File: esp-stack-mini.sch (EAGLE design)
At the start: 43 parts, among them IC1 FT232RL, Q1 200mA/50V, U1 TPS737XX, U2 MCP73831

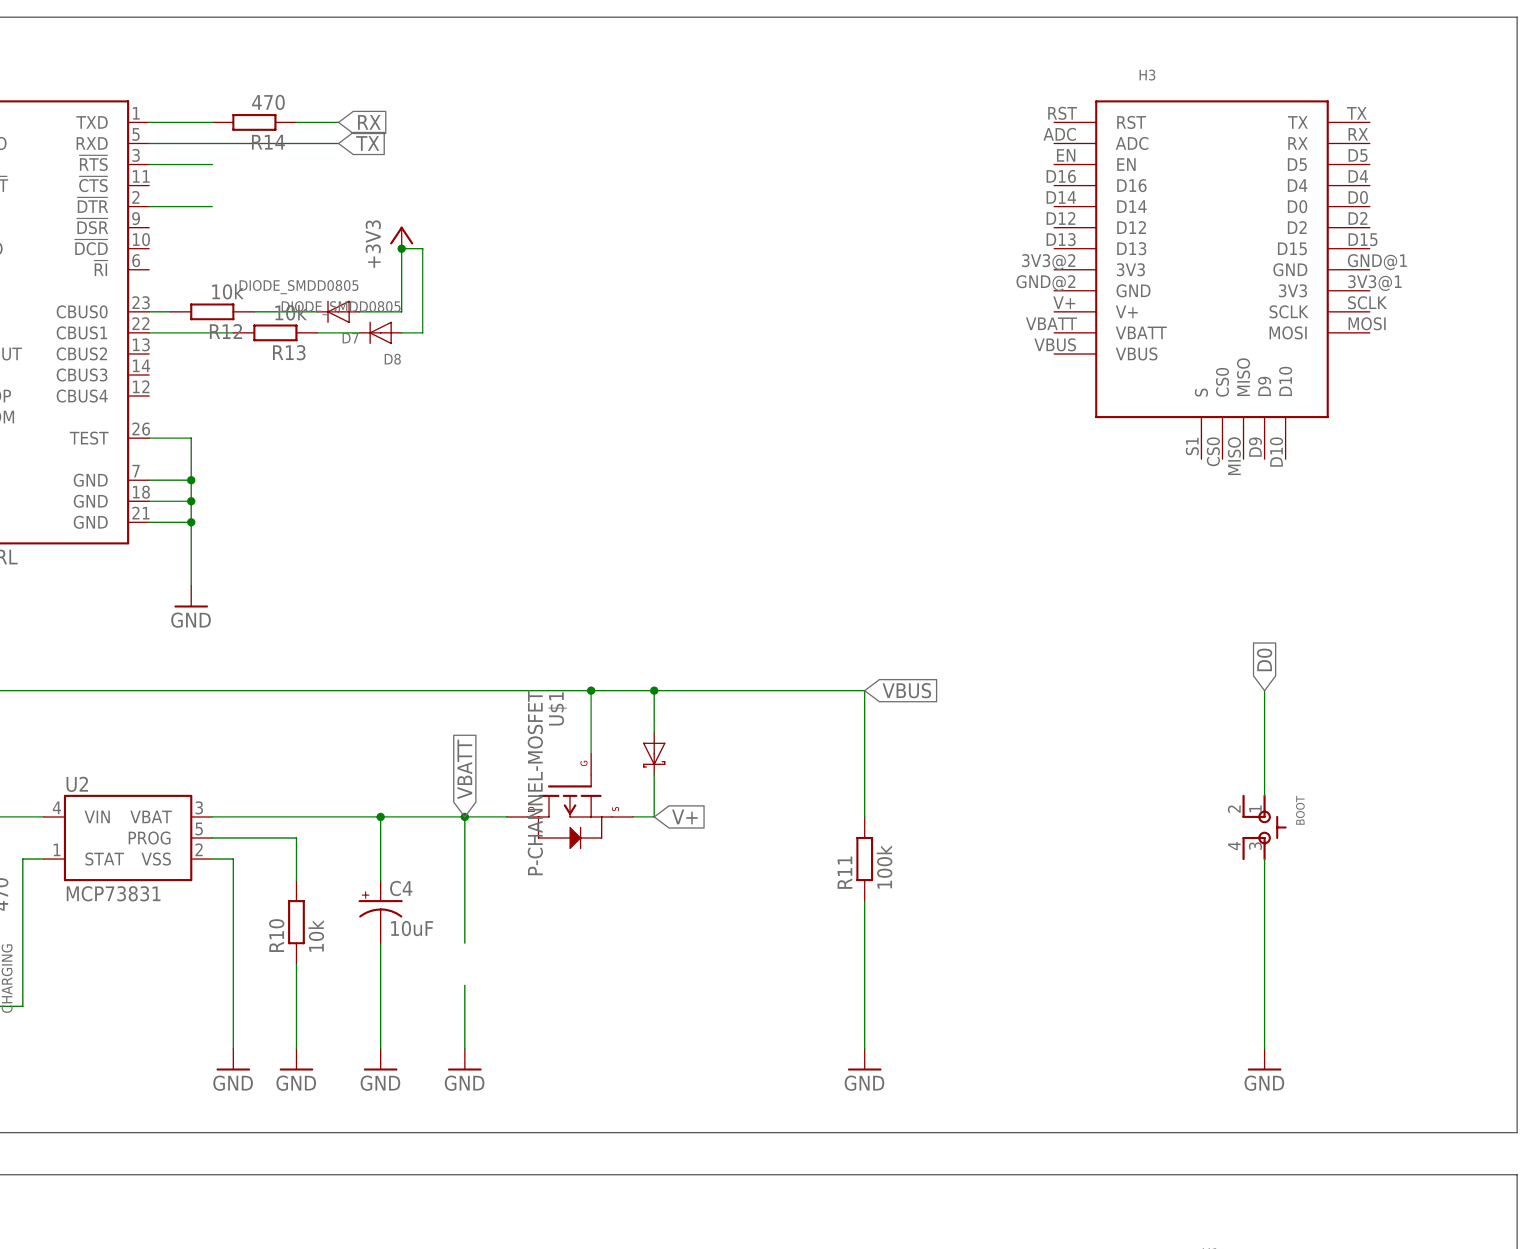
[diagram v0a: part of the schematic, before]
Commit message: USB/Battery board all-connected
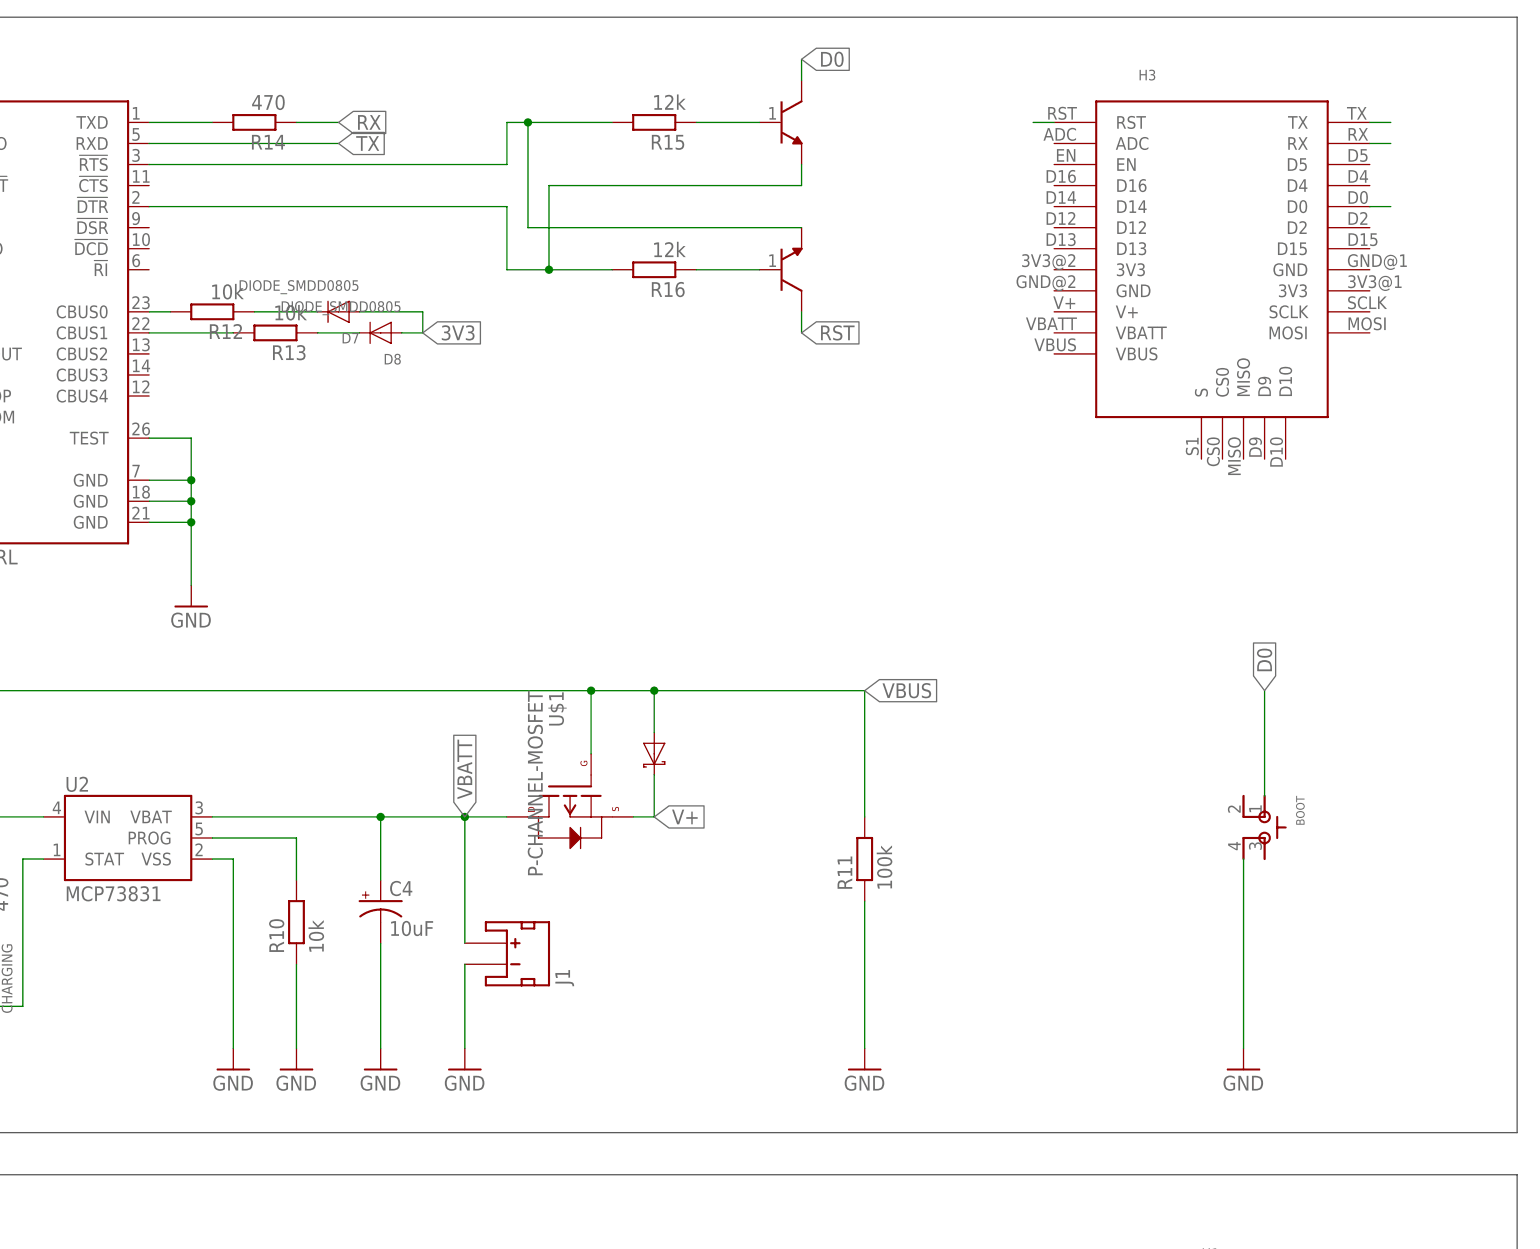
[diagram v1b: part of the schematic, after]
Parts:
- added J1: (no value), SparkFun-Connectors:JST_2MM_MALE
- added R15, R16: 12k, resistor:R-EU_R0805
- added U$2, U$3: NPN-TRANSISTOR, ESPStack-mini:NPN-TRANSISTOR
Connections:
- new net N$8: R16.1, U$3.P$1
- new net N$9: R15.1, U$2.P$1
- net D0: now also H3.D0, U$2.P$3
- net GND: now also BOOT.3, J1.-; no longer BOOT.4
- net N$15: now also R15.2, U$3.P$2
- net N$16: now also R16.2, U$2.P$2
- net RST: now also H3.RST, U$3.P$3
- net RX: now also H3.RX
- net TX: now also H3.TX
- net VBATT: now also J1.+
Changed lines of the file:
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@@
 <part name="R12" library="resistor" deviceset="R-EU_" device="R0805" value="10k"/>
 <part name="R13" library="resistor" deviceset="R-EU_" device="R0805" value="10k"/>
-<part name="3V4" library="supply1" deviceset="+3V3" device=""/>
 <part name="R14" library="resistor" deviceset="R-EU_" device="R0805" value="470"/>
 <part name="C5" library="SparkFun-Capacitors" deviceset="CAP" device="0805"/>
@@
 <part name="GND15" library="supply1" deviceset="GND" device=""/>
 <part name="JP3" library="SparkFun-Connectors" deviceset="USB" device="-MICROB"/>
+<part name="J1" library="SparkFun-Connectors" deviceset="JST_2MM_MALE" device=""/>
+<part name="U$2" library="ESPStack-mini" deviceset="NPN-TRANSISTOR" device=""/>
+<part name="U$3" library="ESPStack-mini" deviceset="NPN-TRANSISTOR" device=""/>
+<part name="R15" library="resistor" deviceset="R-EU_" device="R0805" value="12k"/>
+<part name="R16" library="resistor" deviceset="R-EU_" device="R0805" value="12k"/>
 </parts>
 <sheets>
@@
 <instance part="GND11" gate="1" x="5.08" y="121.92"/>
 <instance part="BOOT" gate="G$1" x="190.5" y="149.86" rot="R270"/>
-<instance part="GND12" gate="1" x="190.5" y="121.92"/>
+<instance part="GND12" gate="1" x="187.96" y="121.92"/>
 <instance part="R12" gate="G$1" x="63.5" y="213.36" rot="R180"/>
 <instance part="R13" gate="G$1" x="71.12" y="210.82" rot="R180"/>
-<instance part="3V4" gate="G$1" x="86.36" y="223.52"/>
 <instance part="R14" gate="G$1" x="68.58" y="236.22" rot="R180"/>
 <instance part="C5" gate="G$1" x="10.16" y="190.5"/>
@@
 <instance part="GND15" gate="1" x="60.96" y="177.8"/>
 <instance part="JP3" gate="G$1" x="-2.54" y="149.86" rot="MR0"/>
+<instance part="J1" gate="G$1" x="99.06" y="134.62" rot="MR90"/>
+<instance part="U$2" gate="G$1" x="132.08" y="236.22"/>
+<instance part="U$3" gate="G$1" x="132.08" y="218.44" rot="MR180"/>
+<instance part="R15" gate="G$1" x="116.84" y="236.22" rot="R180"/>
+<instance part="R16" gate="G$1" x="116.84" y="218.44" rot="R180"/>
 </instances>
 <busses>
@@
 <wire x1="50.8" y1="22.86" x2="50.8" y2="27.94" width="0.1524" layer="91"/>
 <label x="50.8" y="25.4" size="1.4224" layer="95" xref="yes"/>
+</segment>
+<segment>
+<pinref part="H3" gate="G$1" pin="RST"/>
+<wire x1="165.1" y1="236.22" x2="162.56" y2="236.22" width="0.1524" layer="91"/>
+</segment>
+<segment>
+<pinref part="U$3" gate="G$1" pin="P$3"/>
+<wire x1="134.62" y1="213.36" x2="134.62" y2="210.82" width="0.1524" layer="91"/>
+<label x="134.62" y="210.82" size="1.778" layer="95" xref="yes"/>
 </segment>
 </net>
@@
 <wire x1="63.5" y1="152.4" x2="83.82" y2="152.4" width="0.1524" layer="91"/>
 <junction x="83.82" y="152.4"/>
+<pinref part="J1" gate="G$1" pin="+"/>
 </segment>
 </net>
@@
 <pinref part="D8" gate="G$1" pin="A"/>
 <wire x1="86.36" y1="210.82" x2="88.9" y2="210.82" width="0.1524" layer="91"/>
-<wire x1="88.9" y1="210.82" x2="88.9" y2="220.98" width="0.1524" layer="91"/>
+<wire x1="88.9" y1="210.82" x2="88.9" y2="213.36" width="0.1524" layer="91"/>
 <pinref part="D7" gate="G$1" pin="A"/>
-<wire x1="81.28" y1="213.36" x2="86.36" y2="213.36" width="0.1524" layer="91"/>
-<wire x1="86.36" y1="213.36" x2="86.36" y2="220.98" width="0.1524" layer="91"/>
-<wire x1="88.9" y1="220.98" x2="86.36" y2="220.98" width="0.1524" layer="91"/>
-<pinref part="3V4" gate="G$1" pin="+3V3"/>
-<junction x="86.36" y="220.98"/>
+<wire x1="81.28" y1="213.36" x2="88.9" y2="213.36" width="0.1524" layer="91"/>
+<label x="88.9" y="210.82" size="1.778" layer="95" xref="yes"/>
 </segment>
 <segment>
@@
 </segment>
 <segment>
-<wire x1="93.98" y1="132.08" x2="93.98" y2="124.46" width="0.1524" layer="91"/>
+<wire x1="93.98" y1="134.62" x2="93.98" y2="124.46" width="0.1524" layer="91"/>
 <pinref part="GND9" gate="1" pin="GND"/>
+<pinref part="J1" gate="G$1" pin="-"/>
 </segment>
 <segment>
@@
 </segment>
 <segment>
-<pinref part="BOOT" gate="G$1" pin="4"/>
 <pinref part="GND12" gate="1" pin="GND"/>
-<wire x1="190.5" y1="147.32" x2="190.5" y2="124.46" width="0.1524" layer="91"/>
+<pinref part="BOOT" gate="G$1" pin="3"/>
+<wire x1="187.96" y1="147.32" x2="187.96" y2="124.46" width="0.1524" layer="91"/>
 </segment>
 <segment>
@@
 <label x="190.5" y="167.64" size="1.778" layer="95" rot="R90" xref="yes"/>
 </segment>
+<segment>
+<pinref part="H3" gate="G$1" pin="D0"/>
+<wire x1="203.2" y1="226.06" x2="205.74" y2="226.06" width="0.1524" layer="91"/>
+</segment>
+<segment>
+<pinref part="U$2" gate="G$1" pin="P$3"/>
+<wire x1="134.62" y1="241.3" x2="134.62" y2="243.84" width="0.1524" layer="91"/>
+<label x="134.62" y="243.84" size="1.778" layer="95" xref="yes"/>
+</segment>
 </net>
 <net name="D4" class="0">
@@
 <label x="78.74" y="236.22" size="1.778" layer="95" xref="yes"/>
 </segment>
+<segment>
+<pinref part="H3" gate="G$1" pin="RX"/>
+<wire x1="203.2" y1="233.68" x2="205.74" y2="233.68" width="0.1524" layer="91"/>
+</segment>
 </net>
 <net name="TX" class="0">
@@
 <wire x1="55.88" y1="233.68" x2="78.74" y2="233.68" width="0.1524" layer="91"/>
 <label x="78.74" y="233.68" size="1.778" layer="95" xref="yes"/>
+</segment>
+<segment>
+<pinref part="H3" gate="G$1" pin="TX"/>
+<wire x1="203.2" y1="236.22" x2="205.74" y2="236.22" width="0.1524" layer="91"/>
 </segment>
 </net>
@@
 <segment>
 <pinref part="IC1" gate="1" pin="!RTS"/>
-<wire x1="55.88" y1="231.14" x2="63.5" y2="231.14" width="0.1524" layer="91"/>
+<wire x1="55.88" y1="231.14" x2="99.06" y2="231.14" width="0.1524" layer="91"/>
+<wire x1="99.06" y1="231.14" x2="99.06" y2="236.22" width="0.1524" layer="91"/>
+<pinref part="R15" gate="G$1" pin="2"/>
+<wire x1="99.06" y1="236.22" x2="101.6" y2="236.22" width="0.1524" layer="91"/>
+<pinref part="U$3" gate="G$1" pin="P$2"/>
+<wire x1="101.6" y1="236.22" x2="111.76" y2="236.22" width="0.1524" layer="91"/>
+<wire x1="134.62" y1="223.52" x2="101.6" y2="223.52" width="0.1524" layer="91"/>
+<wire x1="101.6" y1="223.52" x2="101.6" y2="236.22" width="0.1524" layer="91"/>
+<junction x="101.6" y="236.22"/>
 </segment>
 </net>
@@
 <segment>
 <pinref part="IC1" gate="1" pin="!DTR"/>
-<wire x1="55.88" y1="226.06" x2="63.5" y2="226.06" width="0.1524" layer="91"/>
+<wire x1="55.88" y1="226.06" x2="99.06" y2="226.06" width="0.1524" layer="91"/>
+<wire x1="99.06" y1="226.06" x2="99.06" y2="218.44" width="0.1524" layer="91"/>
+<pinref part="R16" gate="G$1" pin="2"/>
+<wire x1="99.06" y1="218.44" x2="104.14" y2="218.44" width="0.1524" layer="91"/>
+<wire x1="104.14" y1="218.44" x2="111.76" y2="218.44" width="0.1524" layer="91"/>
+<wire x1="104.14" y1="218.44" x2="104.14" y2="228.6" width="0.1524" layer="91"/>
+<junction x="104.14" y="218.44"/>
+<pinref part="U$2" gate="G$1" pin="P$2"/>
+<wire x1="104.14" y1="228.6" x2="134.62" y2="228.6" width="0.1524" layer="91"/>
+<wire x1="134.62" y1="228.6" x2="134.62" y2="231.14" width="0.1524" layer="91"/>
 </segment>
 </net>
@@
 </segment>
 </net>
+<net name="N$8" class="0">
+<segment>
+<pinref part="R16" gate="G$1" pin="1"/>
+<pinref part="U$3" gate="G$1" pin="P$1"/>
+<wire x1="121.92" y1="218.44" x2="129.54" y2="218.44" width="0.1524" layer="91"/>
+</segment>
+</net>
+<net name="N$9" class="0">
+<segment>
+<pinref part="R15" gate="G$1" pin="1"/>
+<pinref part="U$2" gate="G$1" pin="P$1"/>
+<wire x1="121.92" y1="236.22" x2="129.54" y2="236.22" width="0.1524" layer="91"/>
+</segment>
+</net>

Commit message: First prototype
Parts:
- added 1WIRE: (no value), SparkFun-Connectors:M03PTH
- added DHT11/22, HX711: (no value), SparkFun-Connectors:M04NO_SILK_ALL_ROUND
- added H4, H5, H6, H7, H8: ESP-BOARD, ESPStack-mini:ESP-BOARD
- added MODE: (no value), SparkFun-Retired:SOLDERJUMPER_2WAYT
- added R17, R18: 470, resistor:R-EU_R0805
- added R19: 4k7, resistor:R-EU_R0805
- added SJ1: SLEEP, jumper:SJ
- C5: value (none) -> 100nF
- D5: value SCHOTTKY_DIODE_SMDSOD123 -> MBR120
- D7: value DIODE_SMDD0805 -> TX
- D8: value DIODE_SMDD0805 -> RX
- Q1: value 200mA/50V -> BSS138
- Q2: value P-CHANNEL-MOSFET -> AO3401
- Q3, Q4: value NPN-TRANSISTOR -> S8050
- R1, R2, R3, R4, R5, R6, R7, R8: device resistor:R-EU_R1206 -> resistor:R-EU_R0805
- renumbered U$1 to Q2, U$2 to Q3, U$3 to Q4
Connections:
- new net 1WIRE: 1WIRE.2, MODE.3
- new net DHT: DHT11/22.2, MODE.1
- net 3V3: now also 1WIRE.1, DHT11/22.1, HX711.1, R19.2
- net ADC: now also H3.ADC, H6.ADC, H7.ADC, H8.ADC, R17.1, R18.2
- net D0: now also H6.D0, H7.D0, H8.D0
- net D10: now also H6.D10, H7.D10, H8.D10; no longer B1.2, H2.D10, R6.1
- net D12: now also H4.D12, H6.D12, H7.D12, H8.D12, HX711.2
- net D13: now also H2.D13, H6.D13, H7.D13, H8.D13, Q1.S, R7.1
- net D14: now also H4.D14, H6.D14, H7.D14, H8.D14, HX711.3
- net D15: now also H5.D15, H6.D15, H7.D15, H8.D15, MODE.2, R19.1
- net D16: now also H3.D16, H6.D16, H7.D16, H8.D16, SJ1.2
- net D2: now also B1.2, H2.D2, H6.D2, H7.D2, H8.D2, R6.1
- net D4: now also H6.D4, H7.D4, H8.D4
- net D5: now also H6.D5, H7.D5, H8.D5
- net D9: now also H6.D9, H7.D9, H8.D9; no longer H2.D9, Q1.S, R7.1
- net GND: now also 1WIRE.3, DHT11/22.4, HX711.4, R18.1
- net RST: now also SJ1.1
- net S1: now also H6.S, H7.S, H8.S
- net VBATT: now also R17.2
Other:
- note added: "DS18b20 or DHT11/22"
- note added: "HX711"
- note added: "Very thick!"
